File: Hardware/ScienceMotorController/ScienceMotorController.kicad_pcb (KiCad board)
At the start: 2 copper layers, 124.5 x 119.6 mm, 118 parts, among them U1 OKI, U2 TM4C129E_Launchpad, U3 VNH5019A_E, U4 VNH5019A_E, U5 VNH5019A_E, U6 VNH5019A_E, U7 VNH5019A_E, U8 VNH5019A_E

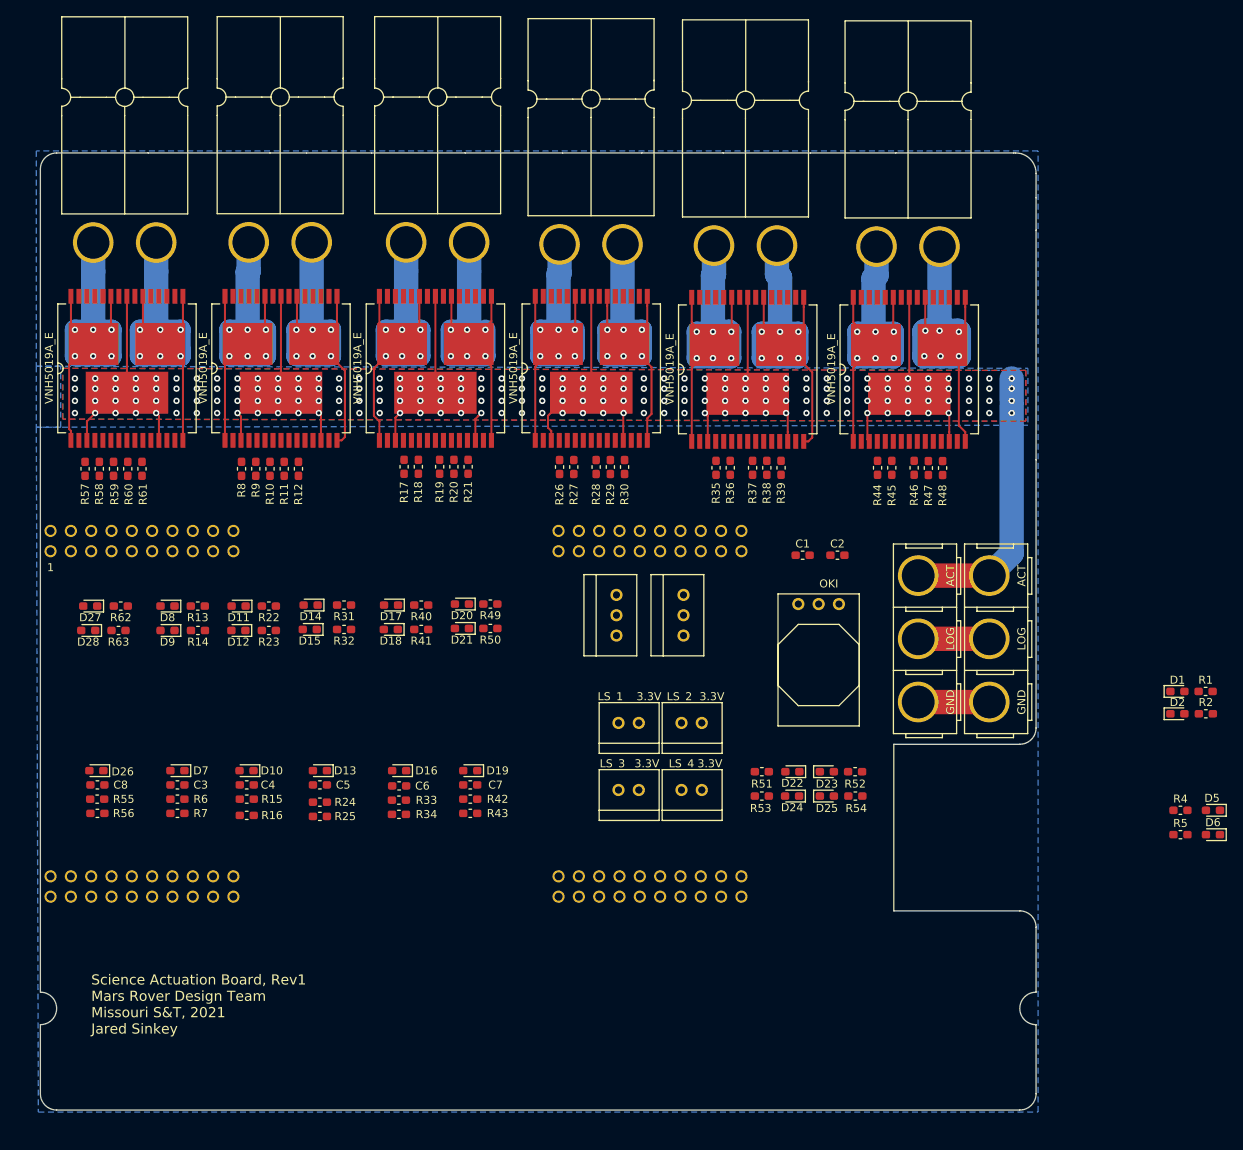
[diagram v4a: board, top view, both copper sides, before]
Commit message: rerouted traces
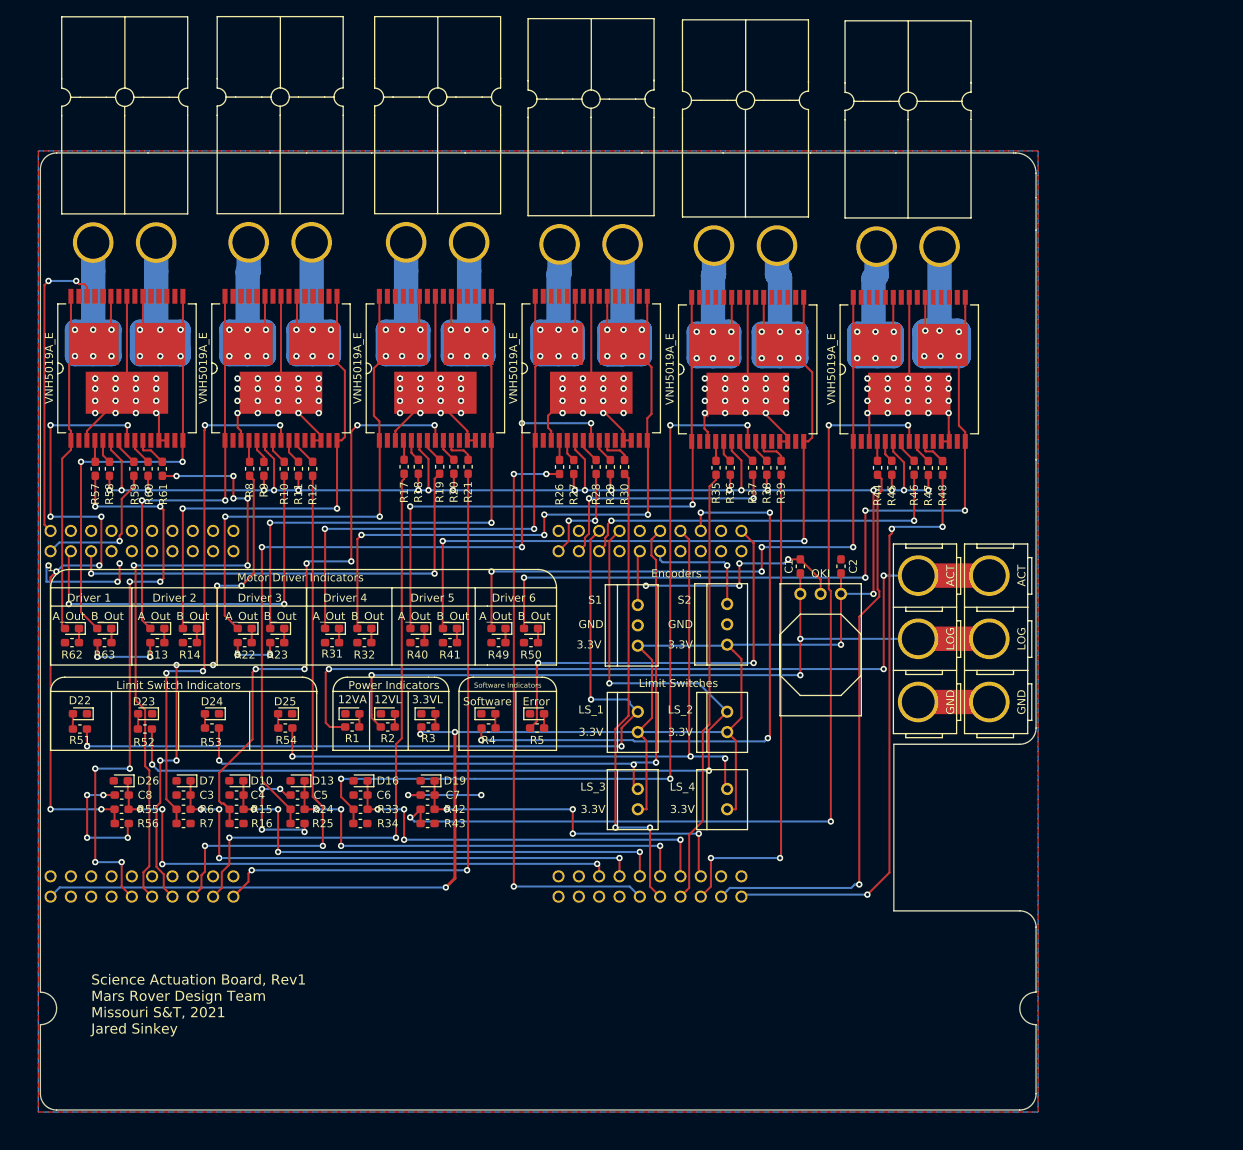
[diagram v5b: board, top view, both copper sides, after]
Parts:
- removed D14, D28, D8: LED, LED_SMD:LED_0603_1608Metric_Pad1.05x0.95mm_HandSolder
- added 3.3VL: LED, LED_SMD:LED_0603_1608Metric_Pad1.05x0.95mm_HandSolder, F.Cu at (83.0, 109.5)
- added A_Out: LED, LED_SMD:LED_0603_1608Metric_Pad1.05x0.95mm_HandSolder, F.Cu at (49.2, 98.8)
- added A_Out: LED, LED_SMD:LED_0603_1608Metric_Pad1.05x0.95mm_HandSolder, F.Cu at (71.0, 98.8)
- added B_Out: LED, LED_SMD:LED_0603_1608Metric_Pad1.05x0.95mm_HandSolder, F.Cu at (42.5, 98.8)
- added R3: 330, Resistor_SMD:R_0603_1608Metric_Pad1.05x0.95mm_HandSolder, F.Cu at (83.0, 111.1)
- moved R1 106.8 mm to (73.5, 111.1), turned to 180 degrees
- moved 12VA 103.2 mm to (73.5, 109.5)
- moved R2 102.3 mm to (78.0, 111.1), turned to 180 degrees
- moved 12VL 98.7 mm to (78.0, 109.5)
- moved Software 91.4 mm to (90.5, 109.5), turned to 0 degrees
- moved D22 89.3 mm to (39.5, 109.5)
- moved R52 88.9 mm to (47.6, 111.4)
- moved R4 87.1 mm to (90.6, 111.3)
- moved Error 85.8 mm to (96.6, 109.5), turned to 0 degrees
- moved D23 85.5 mm to (47.6, 109.5), turned to 180 degrees
- moved R51 85.4 mm to (39.5, 111.4), turned to 180 degrees
- moved R5 81.5 mm to (96.6, 111.3)
- moved D24 73.2 mm to (56.0, 109.5)
- moved R54 71.8 mm to (65.2, 111.3)
- moved R53 69.3 mm to (56.0, 111.3), turned to 180 degrees
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- renumbered D1 to 12VA, D2 to 12VL, D11 to A_Out, D17 to A_Out, D20 to A_Out, D27 to A_Out, D9 to B_Out, D12 to B_Out, D15 to B_Out, D18 to B_Out, D21 to B_Out, D6 to Error, D5 to Software
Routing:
- net /Power/3.3V: track 0.00 -> 373.6 mm, vias 0 -> 24
- net GND: track 8.89 -> 147.2 mm, vias 0 -> 23
- net +12VA: track 167.8 -> 289.5 mm, vias 188 -> 111
- net /Tiva/Limit Switches/Limit_Switch_2: track 0.00 -> 118.5 mm, vias 0 -> 3
- net Net-(R42-Pad1): track 0.00 -> 117.9 mm, vias 0 -> 4
- net Net-(R33-Pad1): track 0.00 -> 103.3 mm, vias 0 -> 4
- net /Tiva/Limit Switches/Limit_Switch_1: track 0.00 -> 102.3 mm, vias 0 -> 3
- net Net-(R24-Pad1): track 0.00 -> 94.8 mm, vias 0 -> 4
- net /Tiva/Limit Switches/Limit_Switch_3: track 0.00 -> 91.9 mm, vias 0 -> 3
- net /Tiva/Limit Switches/Limit_Switch_4: track 0.00 -> 90.4 mm, vias 0 -> 3
- net /Power/12V: track 8.89 -> 96.9 mm, vias 0 -> 3
- net Net-(R55-Pad1): track 0.00 -> 81.1 mm, vias 0 -> 8
- net /Tiva/Motor Driver 3/In_B_3: track 0.00 -> 80.8 mm, vias 0 -> 2
- net /Tiva/Motor Driver 1/In_B_1: track 0.00 -> 79.0 mm, vias 0 -> 6
- net Net-(Conn7-Pad1): track 54.6 -> 133.1 mm, vias 6 -> 10
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- added copper zone on F.Cu, net GND
- removed copper zone on B.Cu, net (none)
- removed copper zone on F.Cu, net +12VA
- removed copper zone on B.Cu, net GND
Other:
- board text added: "Driver 1"
- board text added: "Driver 2"
- board text added: "Driver 3"
- board text added: "Driver 4"
- board text added: "Driver 5"
- board text added: "Driver 6"
- board text added: "Encoders"
- board text added: "GND"
- board text added: "Limit Switch Indicators"
- board text added: "Limit Switches"
- board text added: "Motor Driver Indicators"
- board text added: "Power Indicators"
- board text added: "S1"
- board text added: "S2"
- board text added: "Software Indicators"

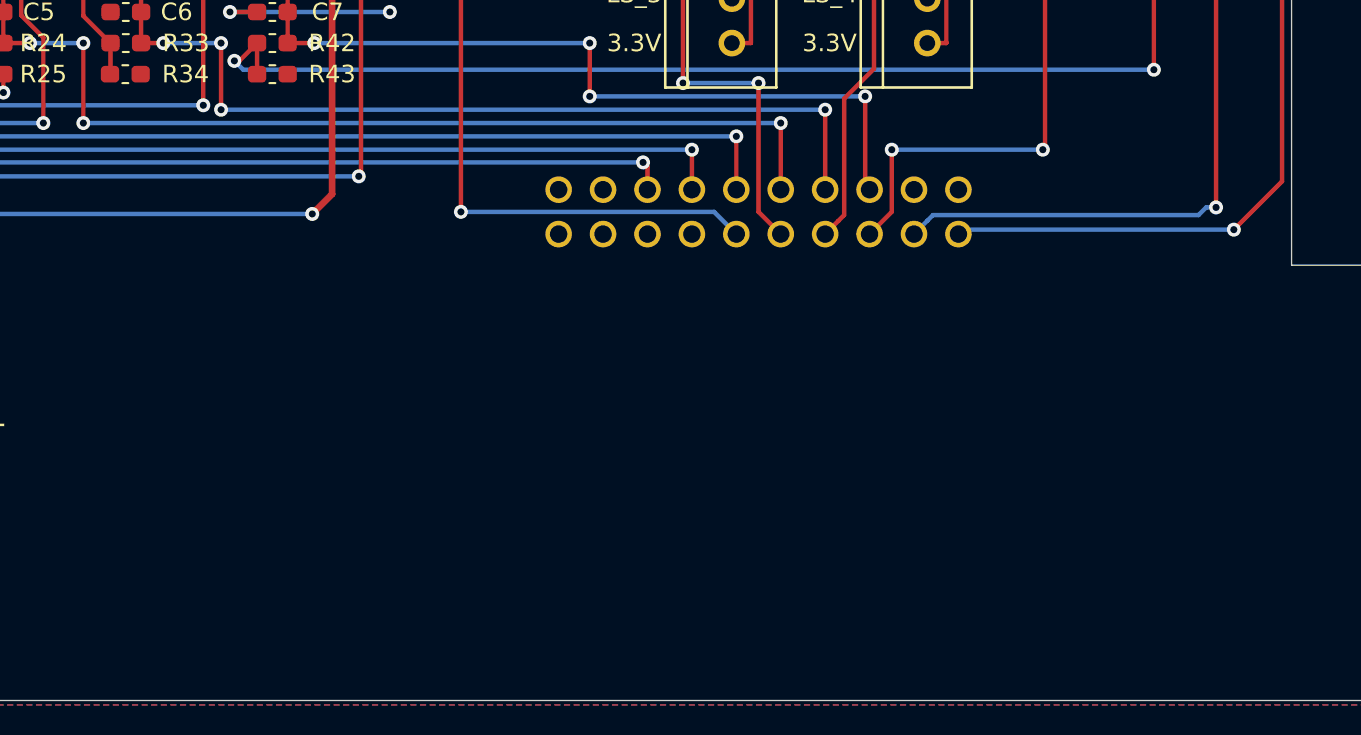
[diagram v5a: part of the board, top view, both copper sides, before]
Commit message: added silkscreens
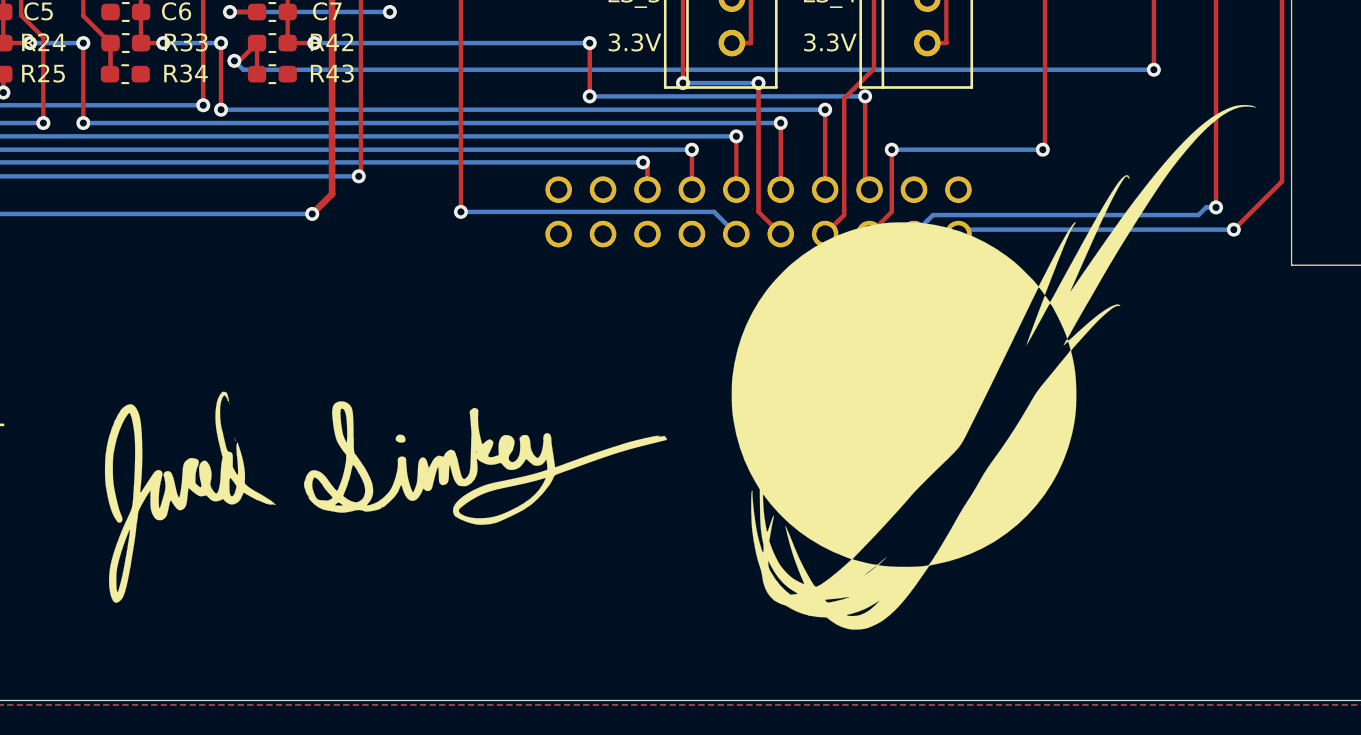
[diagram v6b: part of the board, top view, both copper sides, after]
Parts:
- added G***: LOGO, MRDT_Silkscreens:z_sig_Jared_Sinkey_15.5mmx34.4mm, F.Cu at (89.7, 146.8)
- added G***: LOGO, MRDT_Silkscreens:0_MRDT_Logo_30mm, F.Cu at (124.2, 140.0)

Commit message: Added Gerbs
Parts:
- moved G*** 5.29 mm to (94.0, 149.9)
- moved G*** 1.30 mm to (125.5, 139.7)
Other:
- board text added: "Science Motor Controller Board, Rev1 Mars Rover Design Team Missouri S&T, 2021 Jared Sinkey"
- board text removed: "Science Actuation Board, Rev1 Mars Rover Design Team Missouri S&T, 2021 Jared Sinkey"
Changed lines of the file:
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@@
       (outputformat 1)
       (mirror false)
-      (drillshape 1)
+      (drillshape 0)
       (scaleselection 1)
-      (outputdirectory ""))
+      (outputdirectory "Gerbs/"))
   )
   (net 0 "")
@@
   )
   (module MRDT_Silkscreens:z_sig_Jared_Sinkey_15.5mmx34.4mm (layer F.Cu)
-    (at 89.662 146.812 90)
+    (at 93.98 149.86 90)
     (fp_text reference G*** (at 0 0 90) (layer F.SilkS) hide
       (effects (font (size 1.524 1.524) (thickness 0.3)))
@@
   )
   (module MRDT_Silkscreens:0_MRDT_Logo_30mm (layer F.Cu)
-    (at 124.206 139.954)
+    (at 125.476 139.7)
     (tags "Logo, MRDT")
     (fp_text reference G*** (at -4.6228 17.8054) (layer Dwgs.User) hide
@@
     (effects (font (size 1 1) (thickness 0.15)))
   )
-  (gr_text "Science Actuation Board, Rev1\nMars Rover Design Team\nMissouri S&T, 2021\nJared Sinkey" (at 40.894 145.796) (layer F.SilkS)
+  (gr_text "Science Motor Controller Board, Rev1\nMars Rover Design Team\nMissouri S&T, 2021\nJared Sinkey" (at 40.894 145.796) (layer F.SilkS)
     (effects (font (size 1.27 1.27) (thickness 0.15)) (justify left))
   )

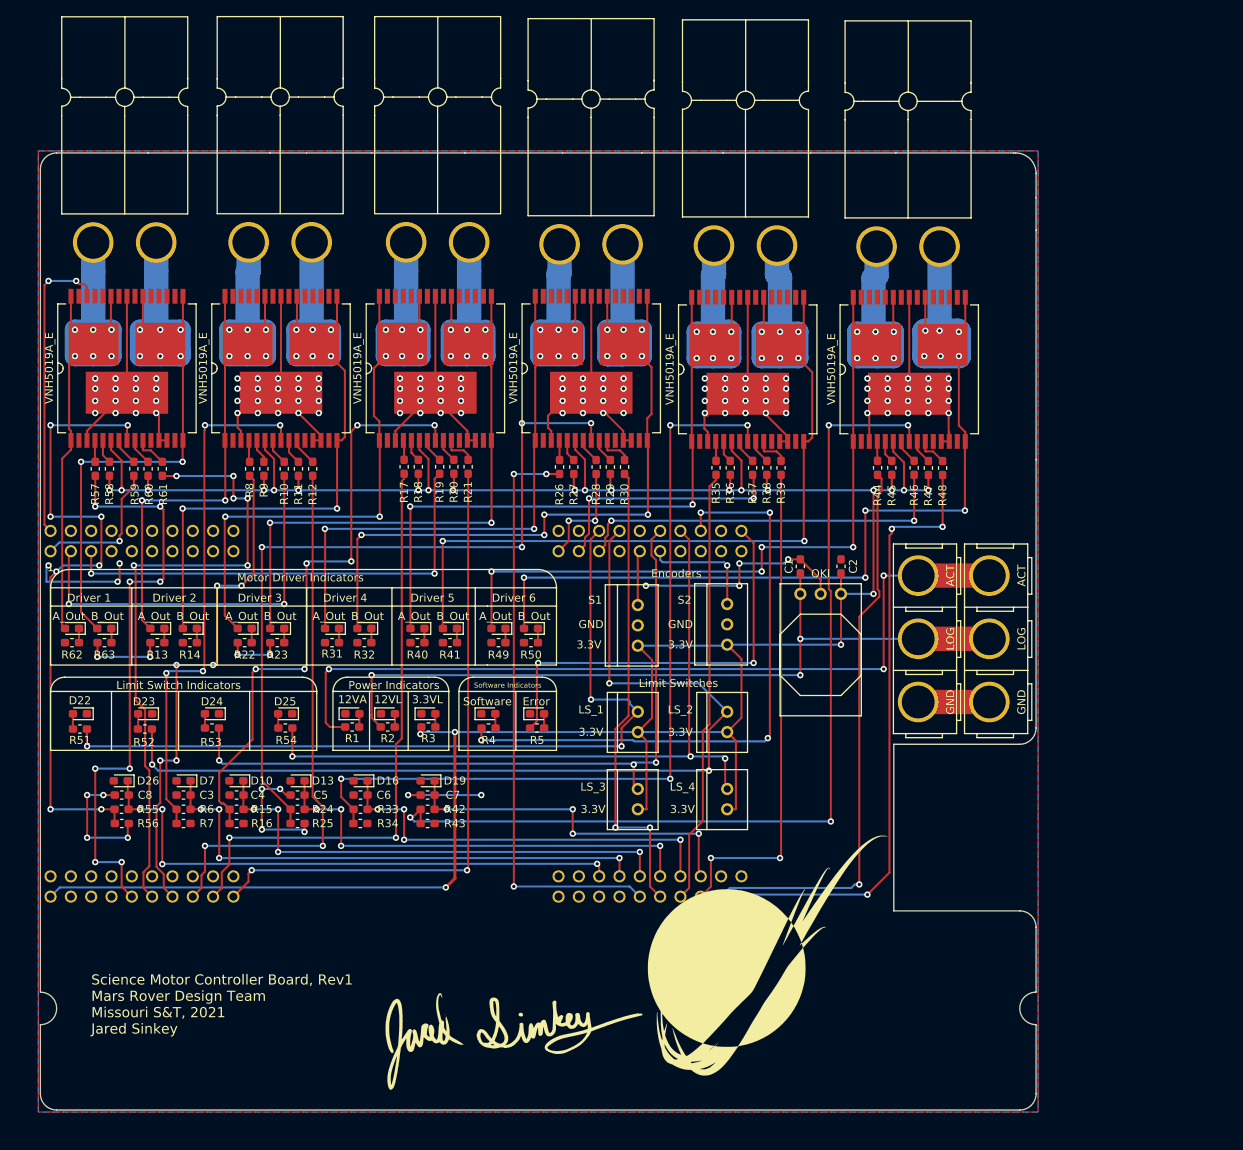
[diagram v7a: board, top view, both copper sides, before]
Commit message: added ground plane and 12VA plane
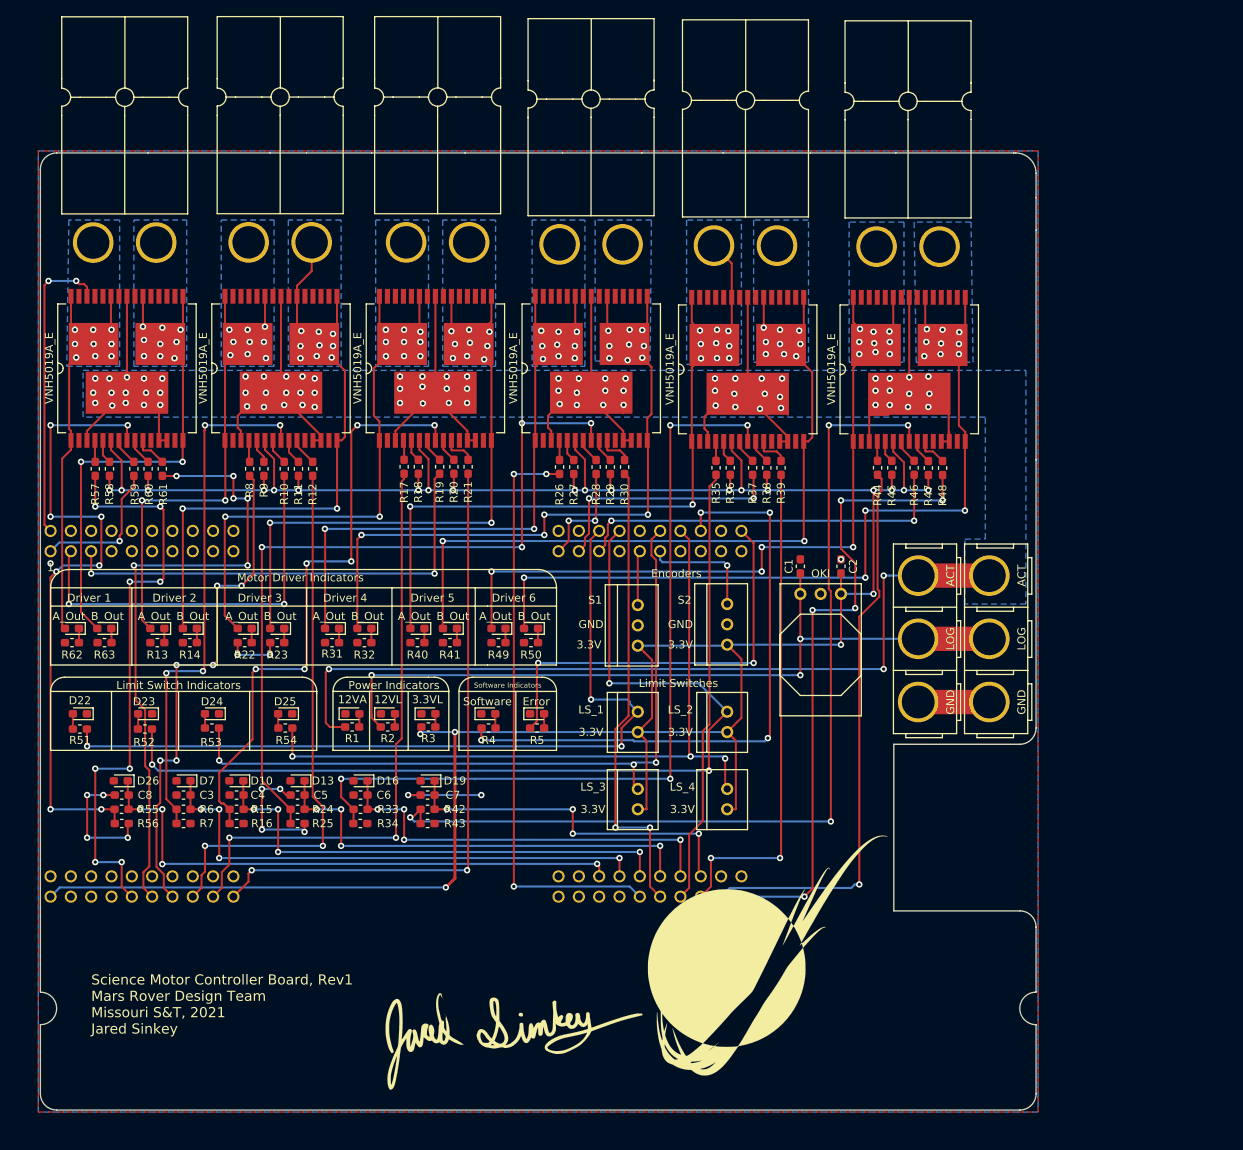
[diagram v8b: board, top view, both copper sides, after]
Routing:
- net GND: track 147.2 -> 96.0 mm, vias 23 -> 16
- net Net-(Conn12-Pad1): track 96.1 -> 62.0 mm, vias 8 -> 11
- net Net-(Conn5-Pad1): track 118.6 -> 87.5 mm, vias 10 -> 13
- net Net-(Conn4-Pad2): track 100.4 -> 71.7 mm, vias 8 -> 11
- net Net-(Conn12-Pad2): track 75.1 -> 46.4 mm, vias 6 -> 9
- net Net-(Conn3-Pad2): track 90.8 -> 62.3 mm, vias 8 -> 11
- net Net-(Conn7-Pad2): track 124.1 -> 95.8 mm, vias 10 -> 13
- net Net-(Conn6-Pad1): track 125.4 -> 97.2 mm, vias 8 -> 11
- net Net-(Conn7-Pad1): track 133.1 -> 106.0 mm, vias 10 -> 13
- net Net-(Conn4-Pad1): track 105.8 -> 79.4 mm, vias 8 -> 11
- net Net-(Conn5-Pad2): track 103.2 -> 77.2 mm, vias 8 -> 11
- net Net-(Conn6-Pad2): track 114.0 -> 93.2 mm, vias 8 -> 11
- net Net-(Conn3-Pad1): track 99.5 -> 79.2 mm, vias 8 -> 11
- net +12VA: track 289.5 -> 294.8 mm, vias 111 -> 81
- net /Tiva/Motor Driver 6/In_B_6: track 75.8 -> 80.0 mm, vias 3 -> 5
- added copper zone on B.Cu, net GND
- added copper zone on B.Cu, net Net-(Conn12-Pad1)
- added copper zone on B.Cu, net Net-(Conn12-Pad2)
- added copper zone on B.Cu, net Net-(Conn3-Pad2)
- added copper zone on B.Cu, net Net-(Conn4-Pad1)
- added copper zone on B.Cu, net Net-(Conn4-Pad2)
- added copper zone on B.Cu, net Net-(Conn5-Pad1)
- added copper zone on B.Cu, net Net-(Conn5-Pad2)
- added copper zone on B.Cu, net Net-(Conn6-Pad1)
- added copper zone on B.Cu, net Net-(Conn7-Pad1)
- added copper zone on B.Cu, net Net-(Conn7-Pad2)
